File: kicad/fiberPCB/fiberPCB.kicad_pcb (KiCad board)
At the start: 2 copper layers, 33 x 24 mm, 23 parts, among them J1 Conn_01x01_Male, J2 Conn_01x01_Male, J3 Conn_01x01_Male, J4 Conn_01x01_Male, J5 Conn_01x01_Male, J6 Conn_01x01_Male, J7 Conn_01x01_Male, J8 Conn_01x01_Male, P5 Conn_01x10_Male

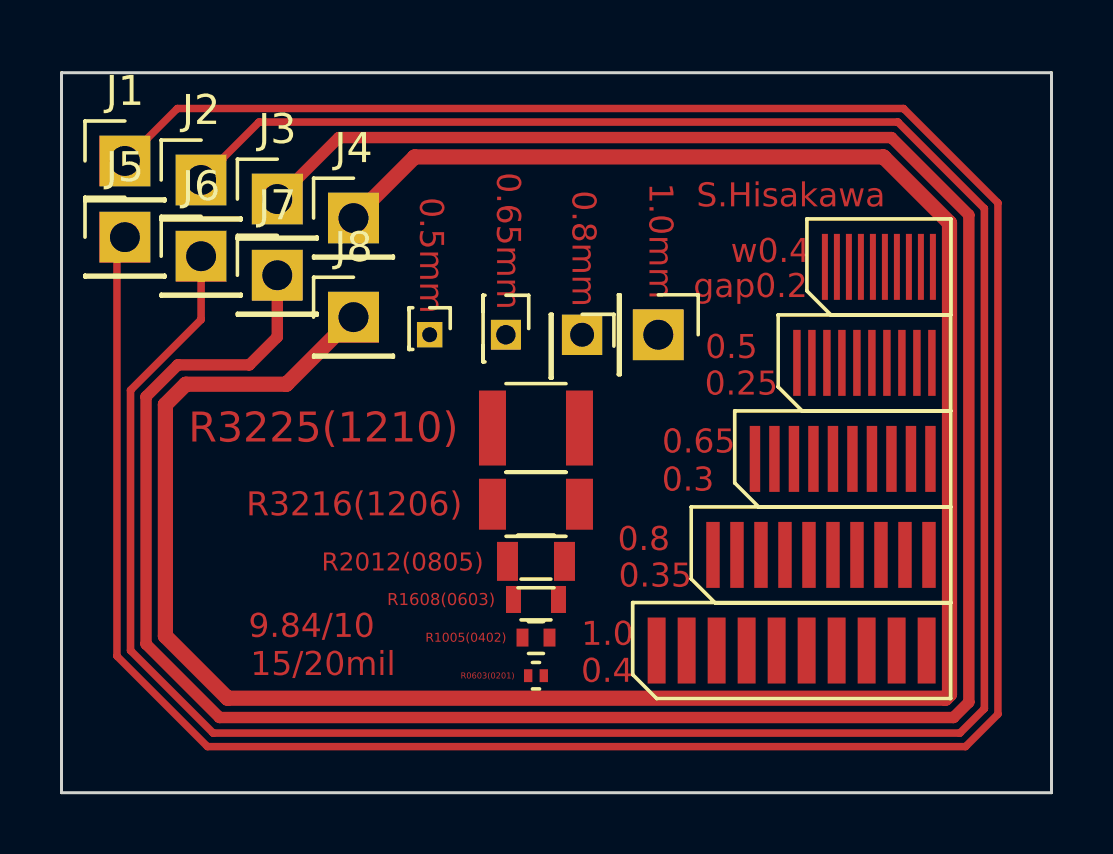
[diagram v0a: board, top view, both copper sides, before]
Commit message: add image of step1
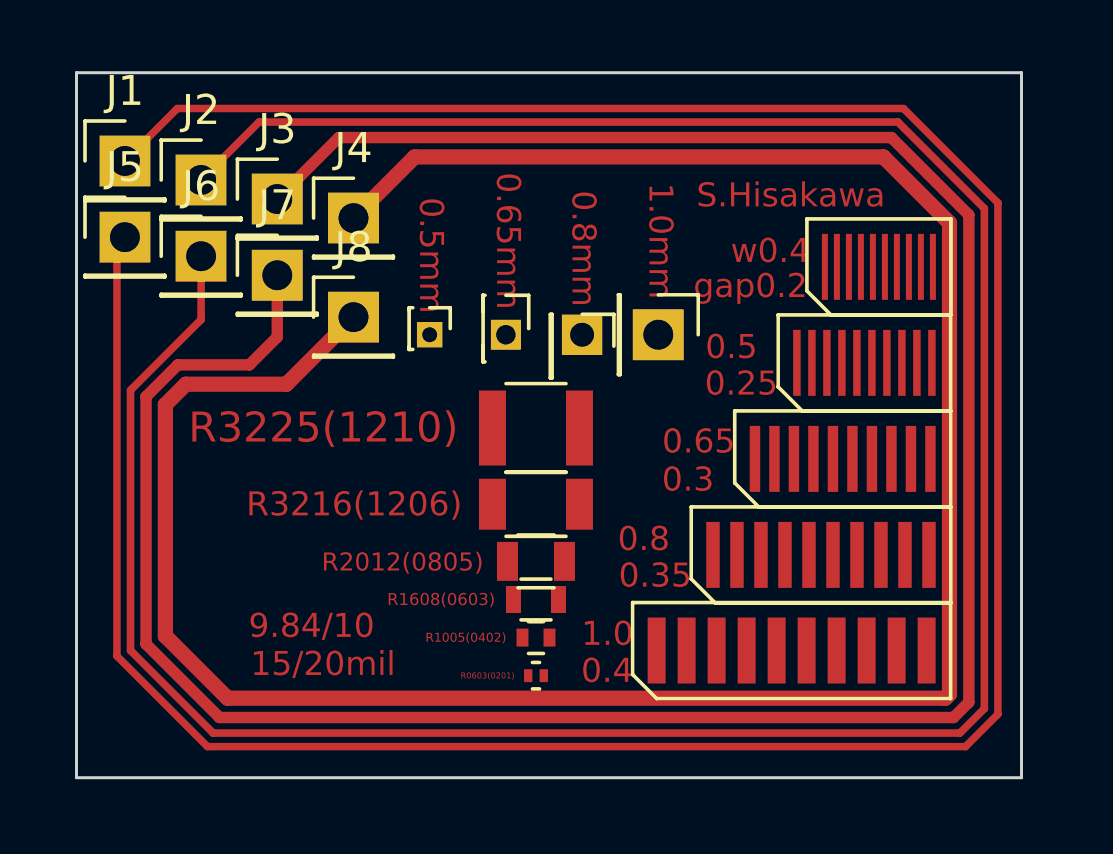
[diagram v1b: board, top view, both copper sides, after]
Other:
- board size 33 x 24 mm -> 31.5 x 23.5 mm
- board text added: "23.5x31.5mm"
- board text removed: "24x33mm"
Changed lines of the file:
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@@
     (45 Margin user)
     (46 B.CrtYd user hide)
-    (47 F.CrtYd user)
+    (47 F.CrtYd user hide)
     (48 B.Fab user hide)
     (49 F.Fab user hide)
@@
     )
   )
-  (gr_text 24x33mm (at 143 32) (layer Dwgs.User)
+  (gr_text 23.5x31.5mm (at 145.5 32) (layer Dwgs.User)
     (effects (font (size 1 1) (thickness 0.15)))
   )
-  (gr_line (start 140 57) (end 140 33) (layer Edge.Cuts) (width 0.1))
-  (gr_line (start 173 57) (end 140 57) (layer Edge.Cuts) (width 0.1))
-  (gr_line (start 173 33) (end 173 57) (layer Edge.Cuts) (width 0.1))
-  (gr_line (start 140 33) (end 173 33) (layer Edge.Cuts) (width 0.1))
+  (gr_line (start 140.5 56.5) (end 140.5 33) (layer Edge.Cuts) (width 0.1))
+  (gr_line (start 172 56.5) (end 140.5 56.5) (layer Edge.Cuts) (width 0.1))
+  (gr_line (start 172 33) (end 172 56.5) (layer Edge.Cuts) (width 0.1))
+  (gr_line (start 140.5 33) (end 172 33) (layer Edge.Cuts) (width 0.1))
   (target plus (at 145.415 49.403) (size 3) (width 0.1) (layer Edge.Cuts))
   (gr_text S.Hisakawa (at 164.3126 37.084) (layer F.Cu)
